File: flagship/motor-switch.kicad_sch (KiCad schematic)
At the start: 12 parts, among them J2 BUS_OUT, Q3 B2B_FET_A, Q4 B2B_FET_B, Q5 PRECHARGE_FET, U2 TPS48111LQ1

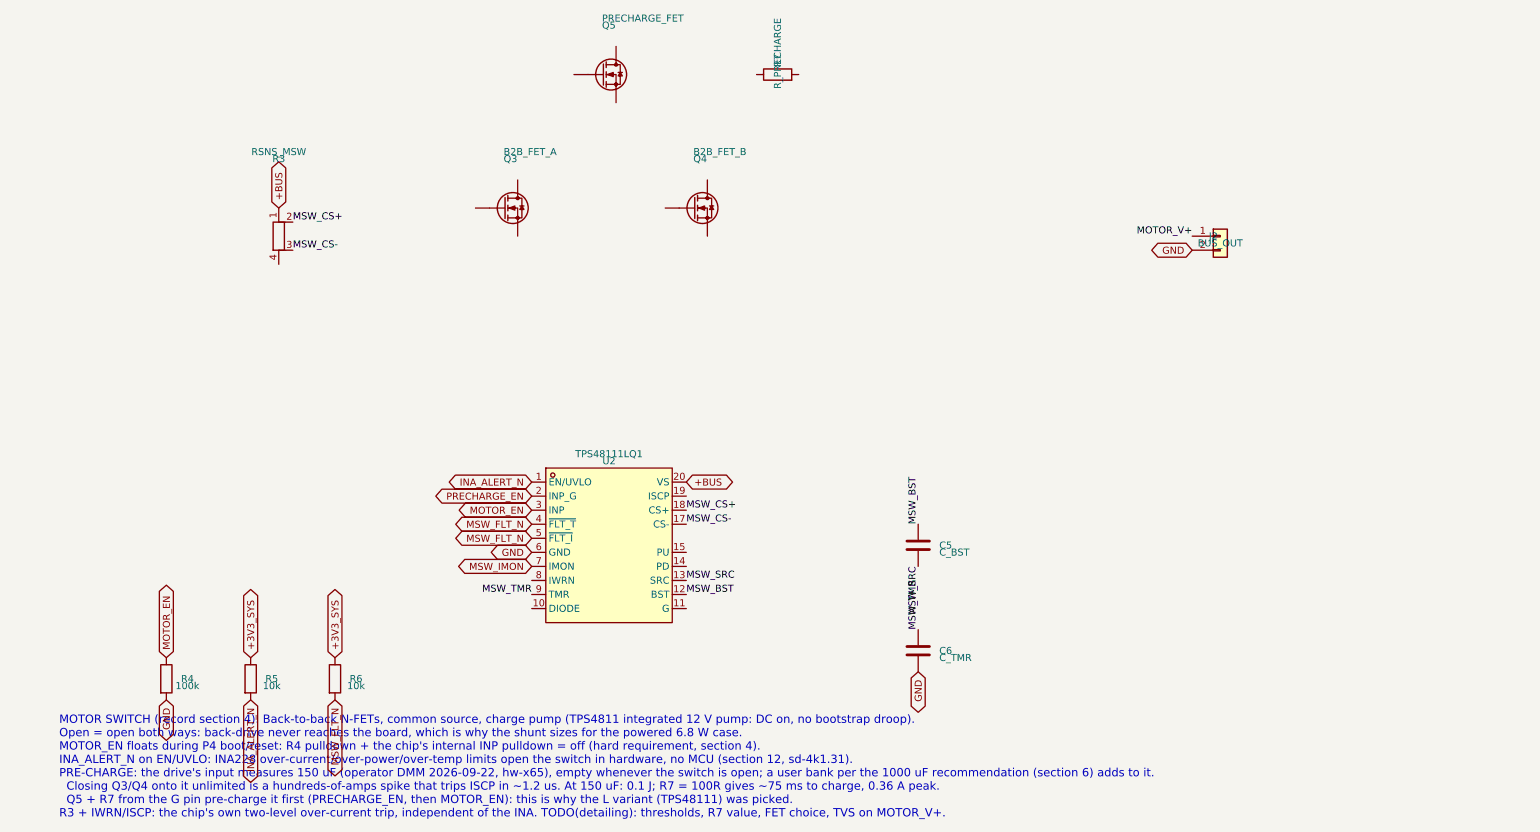
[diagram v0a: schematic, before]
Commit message: flagship: motor switch detailed and drawn as a wired circuit (TPS48111 Figure 9-14)
Back-to-back FETs with the controller rotated so its power pins face the row; every
setting part wired to its pin; labels only for nets leaving the sheet. Values from the
datasheet equations: 2 mOhm sense, OC 15.2 A / 10 ms latch-off, SC 30 A, IMON 3.0 V at
20 A, CBST 470n, UVLO ~23 V, 100 R pre-charge through Q403 + Q402 body diode, MMBT3904
over-temperature, SMBJ48CA output clamp. INA_ALERT_N now pulls a bus-powered EN divider.
Verified: all 22 sheet nets match the intended connection table exactly; ERC 0 errors on
the sheet after typing the TPS48111 pins (PU output, PD passive, FLT open collector).

Co-Authored-By: Claude Opus 5.5 (1M context) <noreply@anthropic.com>
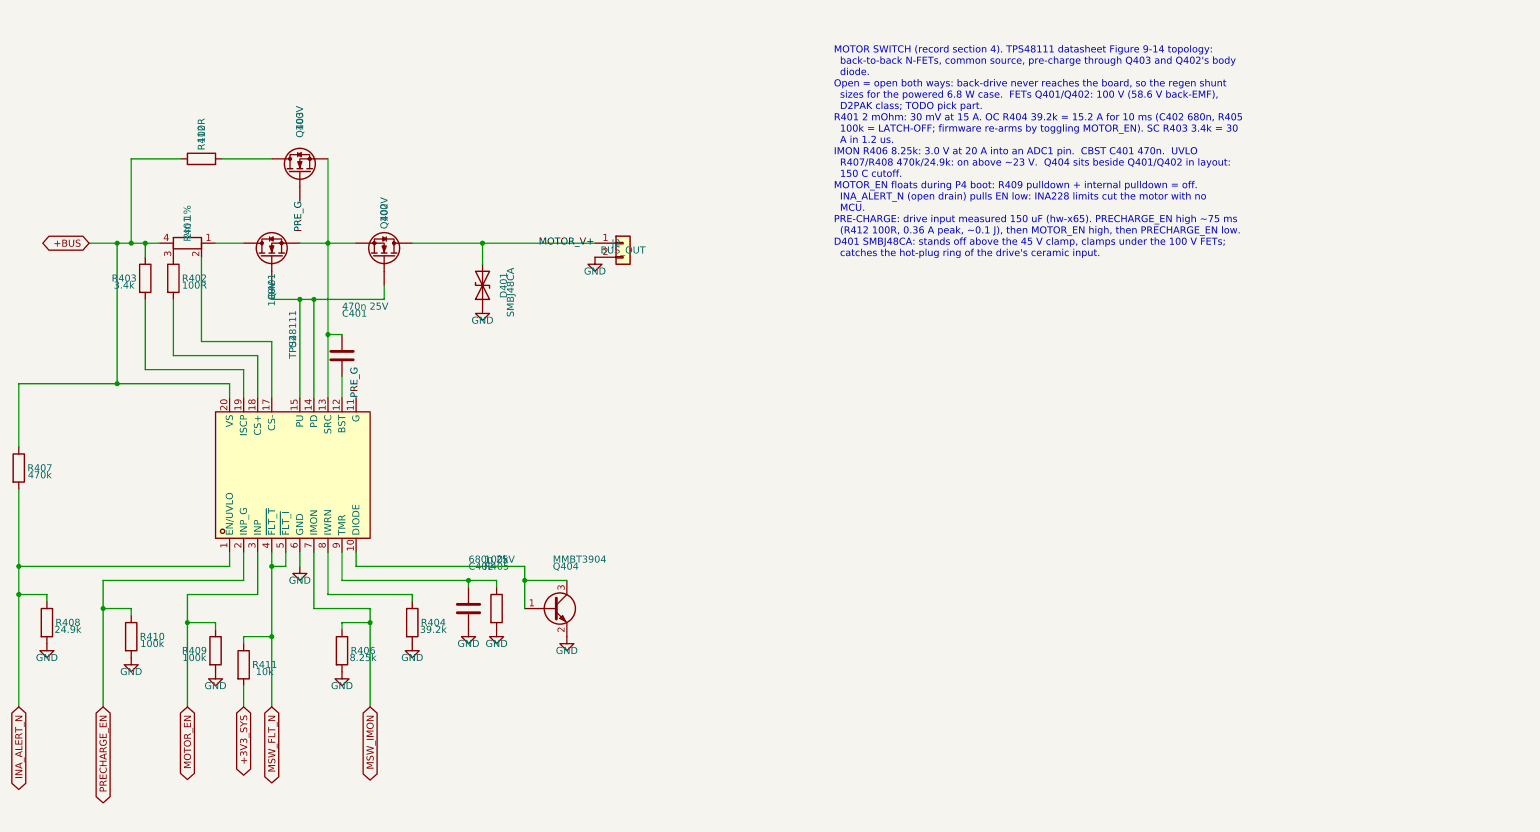
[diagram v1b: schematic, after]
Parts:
- removed C5: C_BST, Capacitor_SMD:C_0805_2012Metric, symbol Device:C
- removed C6: C_TMR, Capacitor_SMD:C_0805_2012Metric, symbol Device:C
- removed Q3: B2B_FET_A, symbol Device:Q_NMOS
- removed Q4: B2B_FET_B, symbol Device:Q_NMOS
- removed Q5: PRECHARGE_FET, symbol Device:Q_NMOS
- removed R3: RSNS_MSW, symbol Device:R_Shunt
- removed R4: 100k, Resistor_SMD:R_0805_2012Metric, symbol Device:R
- removed R5, R6: 10k, Resistor_SMD:R_0805_2012Metric, symbol Device:R
- removed R7: R_PRECHARGE, Resistor_SMD:R_2512_6332Metric, symbol Device:R
- added C401: 470n 25V, Capacitor_SMD:C_0805_2012Metric, symbol Device:C
- added C402: 680n 25V, Capacitor_SMD:C_0805_2012Metric, symbol Device:C
- added D401: SMBJ48CA, Diode_SMD:D_SMB, symbol Device:D_TVS
- added Q401, Q402, Q403: 100V, symbol Device:Q_NMOS
- added Q404: MMBT3904, Package_TO_SOT_SMD:SOT-23, symbol Transistor_BJT:MMBT3904
- added R401: 2m 1%, Resistor_SMD:R_Shunt_Vishay_WSK2512_6332Metric_T1.19mm, symbol Device:R_Shunt
- added R402: 100R, Resistor_SMD:R_0805_2012Metric, symbol Device:R
- added R403: 3.4k, Resistor_SMD:R_0805_2012Metric, symbol Device:R
- added R404: 39.2k, Resistor_SMD:R_0805_2012Metric, symbol Device:R
- added R405, R409, R410: 100k, Resistor_SMD:R_0805_2012Metric, symbol Device:R
- added R406: 8.25k, Resistor_SMD:R_0805_2012Metric, symbol Device:R
- added R407: 470k, Resistor_SMD:R_1206_3216Metric, symbol Device:R
- added R408: 24.9k, Resistor_SMD:R_0805_2012Metric, symbol Device:R
- added R411: 10k, Resistor_SMD:R_0805_2012Metric, symbol Device:R
- added R412: 100R, Resistor_SMD:R_2512_6332Metric, symbol Device:R
- U2: value TPS48111LQ1 -> TPS48111
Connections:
- net +3V3_SYS: now also R411.2
- net +BUS: now also R401.4, R403.1, R407.1, R412.1
- net GND: now also C402.2, D401.1 (A1), Q404.2 (E), R404.2, R405.2, R406.2, R408.2, R409.2, R410.2
- net INA_ALERT_N: now also R407.2, R408.1
- net MOTOR_EN: now also R409.1
- net MOTOR_V+: now also D401.2 (A2), Q402.D
- net MSW_FLT_N: now also R411.1
- net MSW_IMON: now also R406.1
- net PRECHARGE_EN: now also R410.1
- net at U2.10 (DIODE): now also Q404.1 (B), Q404.3 (C)
- net PRE_G: now reaches U2.11 (G)
- net PRE_G: now also Q403.G
- net at U2.14 (PD): now also U2.15 (PU), Q401.G, Q402.G
- net at U2.19 (ISCP): now also R403.2
- net at U2.8 (IWRN): now also R404.1
- net MSW_BST: no longer names the net of U2.12 (BST)
- net MSW_BST: now also C401.2
- net MSW_CS+: no longer names the net of U2.18 (CS+)
- net MSW_CS+: now also R402.2
- net MSW_CS-: no longer names the net of U2.17 (CS-)
- net MSW_CS-: now also R401.2
- net MSW_SRC: no longer names the net of U2.13 (SRC)
- net MSW_SRC: now also C401.1, Q401.S, Q402.S, Q403.S
- net MSW_TMR: no longer names the net of U2.9 (TMR)
- net MSW_TMR: now also C402.1, R405.1
- new net: Q403.D, R412.2
- new net: Q401.D, R401.1
- new net: R401.3, R402.1
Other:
- note added: "MOTOR SWITCH (record section 4). TPS48111 datasheet Figure 9-14 topology: back-to-back N-FETs, common source, pre-charge through Q403 and Q402's body diode. Open = open both ways: back-drive never reaches the board, so the regen shunt sizes for the powered 6.8 W case. FETs Q401/Q402: 100 V (58.6 V back-EMF), D2PAK class; TODO pick part. R401 2 mOhm: 30 mV at 15 A. OC R404 39.2k = 15.2 A for 10 ms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"
- note removed: "MOTOR SWITCH (record section 4). Back-to-back N-FETs, common source, charge pump (TPS4811 integrated 12 V pump: DC on, no bootstrap droop). Open = open both ways: back-drive never reaches the board, which is why the shunt sizes for the powered 6.8 W case. MOTOR_EN floats during P4 boot/reset: R4 pulldown + the chip's internal INP pulldown = off (hard requirement, section 4). INA_ALERT_N on EN/UVL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"

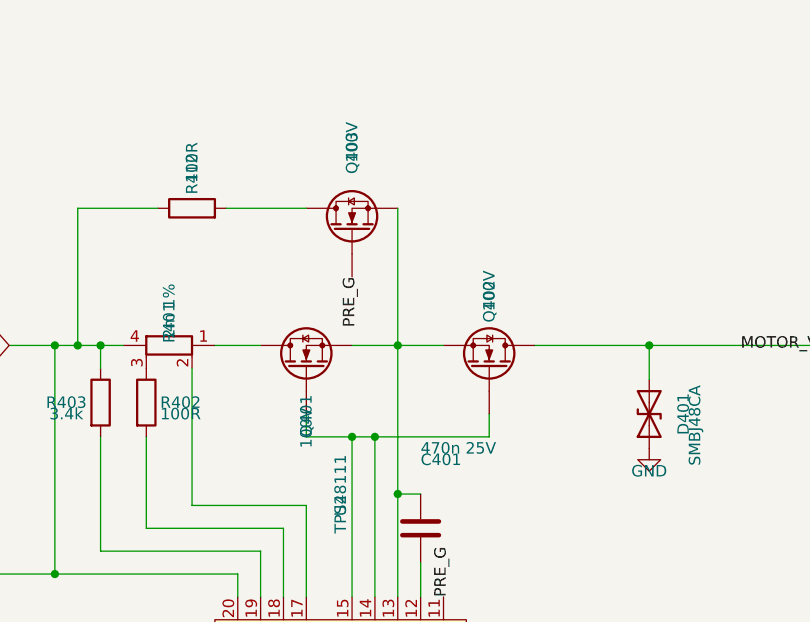
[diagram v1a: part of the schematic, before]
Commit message: flagship: input protection detailed (LTC4364-1); real FETs and regen resistors picked
Input sheet drawn wired from the LTC4364 datasheet Figure 1 topology: 2.5 mOhm / 20 A
limit, 22 nF HGATE soft ramp, 100 nF timer, 51.5 V output clamp above the regen clamp,
UV 20 V / OV 50 V, 15 V gate zeners, SMBJ45CA bidirectional input TVS, 27k fault LED.
Verified: all input nets exact against the intended table; ERC 0 on the sheet.

Parts: PSMN3R7-100BSE (enhanced-SOA hot-swap D2PAK) in all five power FET positions,
DMN10H220L pre-charge FET, 3x Vishay D2TO35M 24 R regen resistors with isolated tabs to
GND. New project symbols with numbered pins matching the footprints: Q_NMOS_D2PAK
(1 G, 2 D tab, 3 S), Q_NMOS_SOT23 (1 G, 2 S, 3 D), R_D2PAK_TAB (resistor 1/3, tab 2).
Regen sheet regenerated for three resistors; nets exact. Motor CBST raised to 1 uF.
ERC: six of seven sheets at zero errors; Compute awaits GPIO assignment by layout.

Co-Authored-By: Claude Opus 5.5 (1M context) <noreply@anthropic.com>
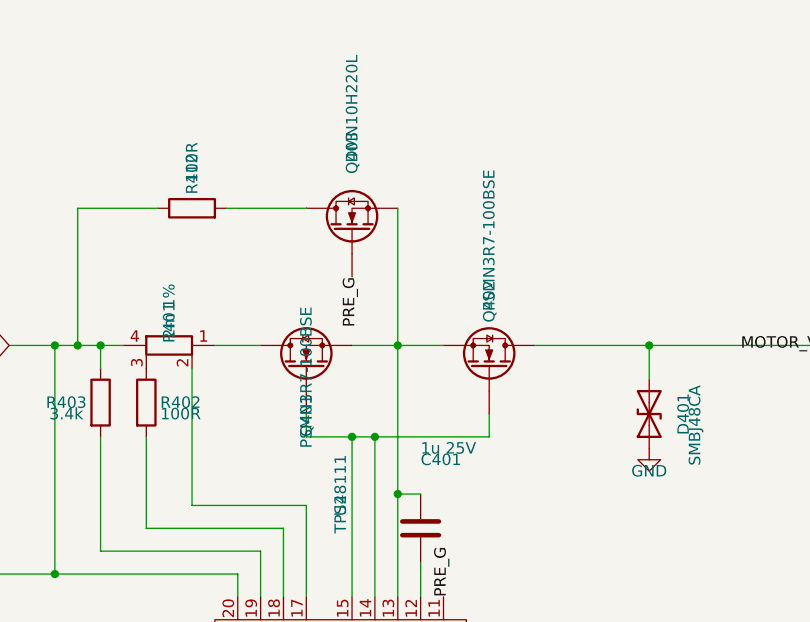
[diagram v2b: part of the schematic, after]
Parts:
- C401: value 470n 25V -> 1u 25V
- Q401, Q402: value 100V -> PSMN3R7-100BSE; footprint (none) -> Package_TO_SOT_SMD:TO-263-2; symbol Device:Q_NMOS -> flagship:Q_NMOS_D2PAK
- Q403: value 100V -> DMN10H220L; footprint (none) -> Package_TO_SOT_SMD:SOT-23; symbol Device:Q_NMOS -> flagship:Q_NMOS_SOT23
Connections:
- net MOTOR_V+: now also Q402.2 (D); no longer Q402.D
- net PRE_G: now also Q403.1 (G); no longer Q403.G
- net at U2.14 (PD), U2.15 (PU): now also Q401.1 (G), Q402.1 (G); no longer Q401.G, Q402.G
- net at R412.2: now also Q403.3 (D); no longer Q403.D
- net at R401.1: now also Q401.2 (D); no longer Q401.D
- new net: C401.1, Q401.3 (S), Q402.3 (S), Q403.2 (S), U2.13 (SRC)
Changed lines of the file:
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@@
 	)
 	(symbol
-		(lib_id "Device:Q_NMOS")
+		(lib_id "flagship:Q_NMOS_D2PAK")
 		(at 78.74 63.5 270)
 		(mirror x)
@@
 			)
 		)
-		(property "Value" "100V"
+		(property "Value" "PSMN3R7-100BSE"
 			(at 78.74 57.15 0)
 			(show_name no)
@@
 			)
 		)
-		(property "Footprint" ""
+		(property "Footprint" "Package_TO_SOT_SMD:TO-263-2"
 			(at 83.82 66.04 0)
 			(hide yes)
@@
 			)
 		)
-		(pin "D"
-		)
-		(pin "G"
-		)
-		(pin "S"
+		(pin "2"
+		)
+		(pin "1"
+		)
+		(pin "3"
 		)
 		(instances
@@
 	)
 	(symbol
-		(lib_id "Device:Q_NMOS")
+		(lib_id "flagship:Q_NMOS_SOT23")
 		(at 63.5 48.26 90)
 		(unit 1)
@@
 			)
 		)
-		(property "Value" "100V"
+		(property "Value" "DMN10H220L"
 			(at 63.5 40.64 0)
 			(show_name no)
@@
 			)
 		)
-		(property "Footprint" ""
+		(property "Footprint" "Package_TO_SOT_SMD:SOT-23"
 			(at 68.58 50.8 0)
 			(hide yes)
@@
 			)
 		)
-		(pin "D"
-		)
-		(pin "G"
-		)
-		(pin "S"
+		(pin "3"
+		)
+		(pin "1"
+		)
+		(pin "2"
 		)
 		(instances
@@
 			)
 		)
-		(property "Value" "470n 25V"
+		(property "Value" "1u 25V"
 			(at 71.12 72.39 0)
 			(show_name no)
@@
 	)
 	(symbol
-		(lib_id "Device:Q_NMOS")
+		(lib_id "flagship:Q_NMOS_D2PAK")
 		(at 58.42 63.5 90)
 		(unit 1)
@@
 			)
 		)
-		(property "Value" "100V"
+		(property "Value" "PSMN3R7-100BSE"
 			(at 58.42 72.39 0)
 			(show_name no)
@@
 			)
 		)
-		(property "Footprint" ""
+		(property "Footprint" "Package_TO_SOT_SMD:TO-263-2"
 			(at 63.5 66.04 0)
 			(hide yes)
@@
 			)
 		)
-		(pin "D"
-		)
-		(pin "G"
-		)
-		(pin "S"
-		)
-		(instances
+		(pin "2"
+		)
+		(pin "1"
+		)
+		(pin "3"
+		)
+		(instances

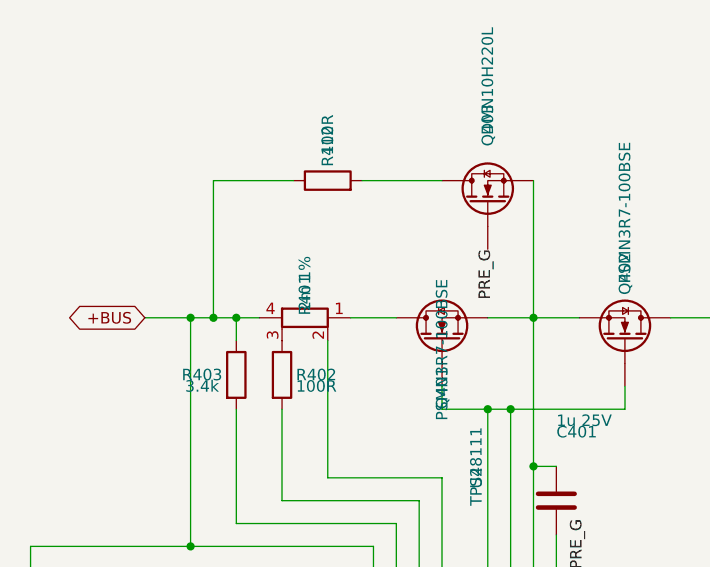
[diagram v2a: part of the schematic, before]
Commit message: flagship: Kelvin WSK2512 shunts everywhere (LTC4364 sense now 4-terminal), bulk and MLCC parts picked
R1 (LTC4364, 2.5 mOhm) becomes a 4-terminal shunt with SENSE and OUT on its Kelvin taps;
R1/R2/R401 all Vishay WSK2512 on the T2.21 mm footprint that value range needs. Bulk:
2x EEH-ZA1J101P 100 uF 63 V hybrid polymer + 2x GRM32ER72A225KA35L; buck input caps get
the same MLCC part number. Regen resistors labeled D2TO35M 24 R 2 %. Input nets verified
exact after regeneration; ERC 0 on every detailed sheet.

Co-Authored-By: Claude Opus 5.5 (1M context) <noreply@anthropic.com>
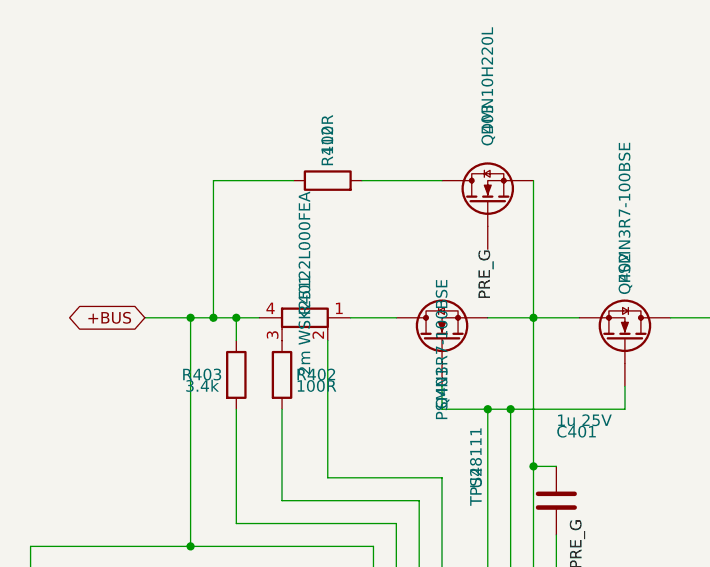
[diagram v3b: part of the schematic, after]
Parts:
- R401: value 2m 1% -> 2m WSK25122L000FEA; footprint Resistor_SMD:R_Shunt_Vishay_WSK2512_6332Metric_T1.19mm -> Resistor_SMD:R_Shunt_Vishay_WSK2512_6332Metric_T2.21mm
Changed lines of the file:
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@@
 			)
 		)
-		(property "Value" "2m 1%"
+		(property "Value" "2m WSK25122L000FEA"
 			(at 43.18 57.15 0)
 			(show_name no)
@@
 			)
 		)
-		(property "Footprint" "Resistor_SMD:R_Shunt_Vishay_WSK2512_6332Metric_T1.19mm"
+		(property "Footprint" "Resistor_SMD:R_Shunt_Vishay_WSK2512_6332Metric_T2.21mm"
 			(at 41.4 60.96 90)
 			(hide yes)
